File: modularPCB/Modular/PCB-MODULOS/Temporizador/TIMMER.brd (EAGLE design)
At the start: 38 x 33 mm, 8 parts

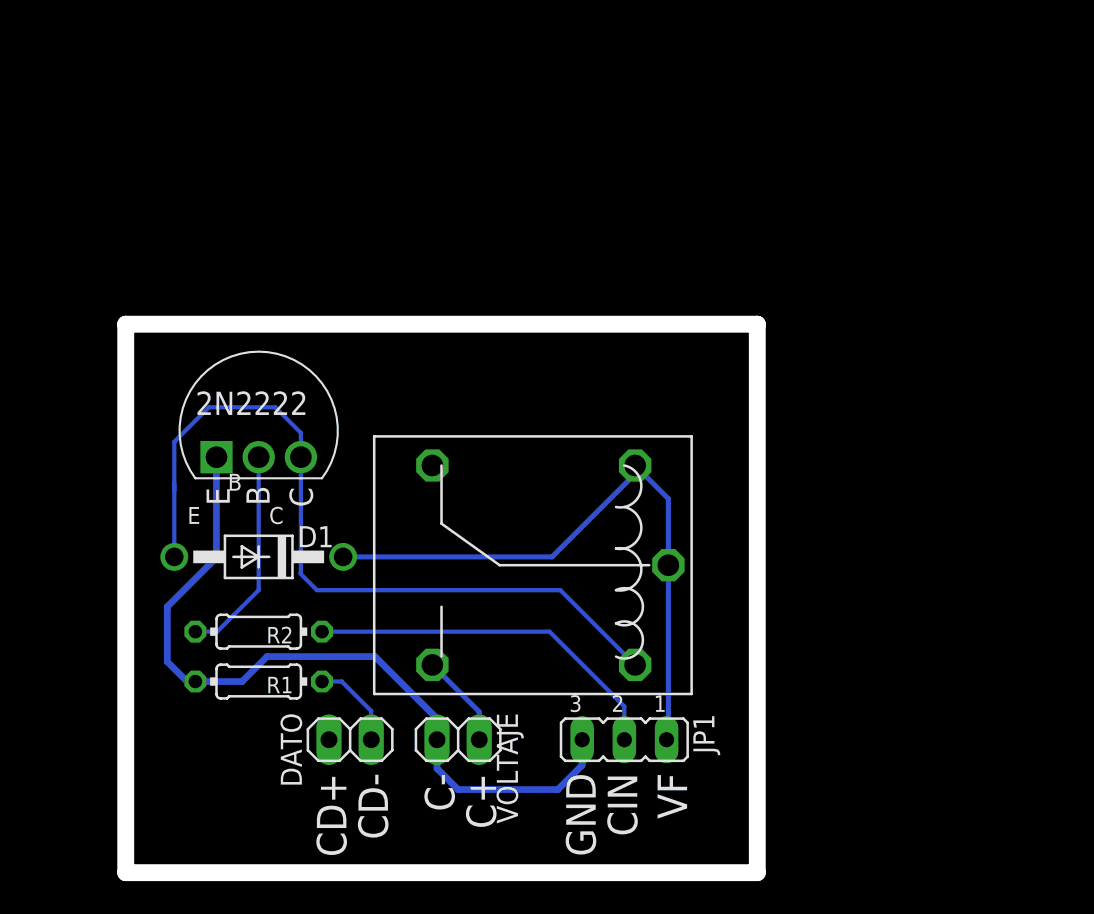
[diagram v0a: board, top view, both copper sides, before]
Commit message: Corrección de errores en pcbs
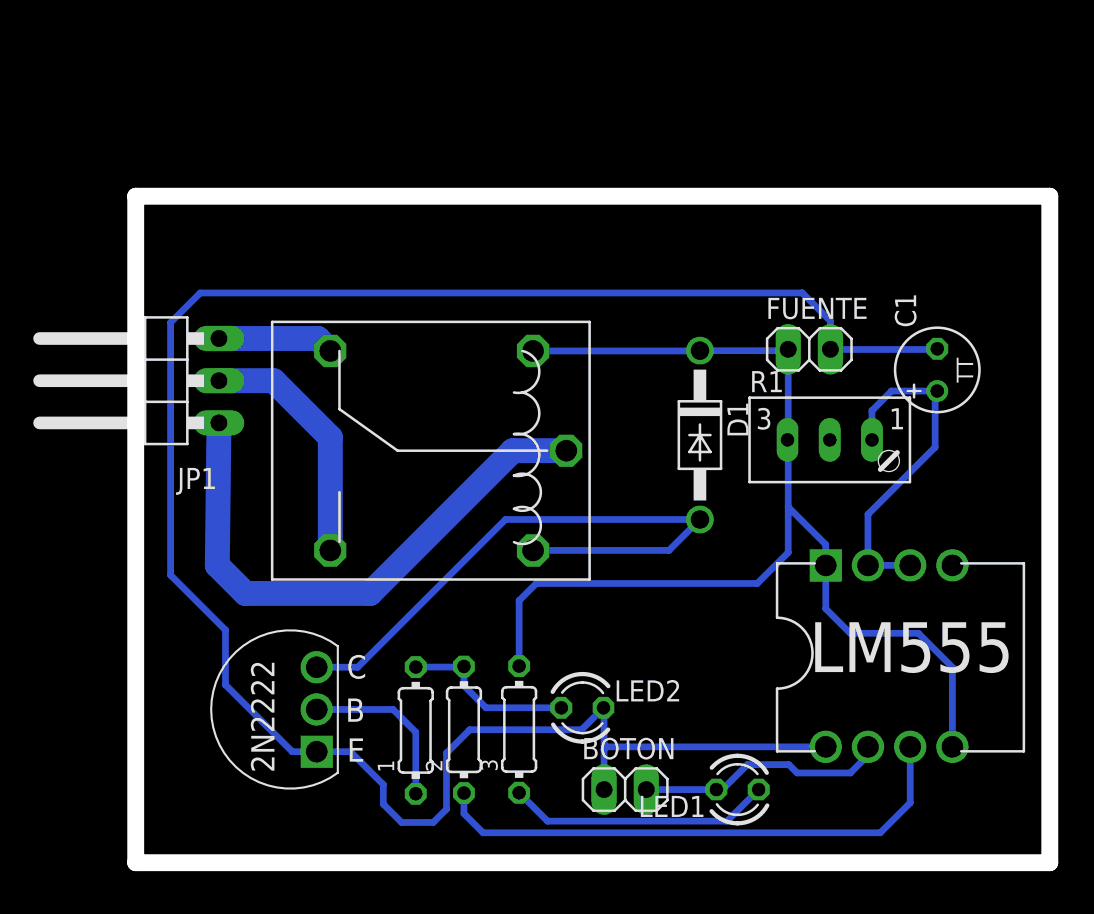
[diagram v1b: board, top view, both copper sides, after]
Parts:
- removed DATO, VOLTAJE: (no value), pinhead:1X02
- removed R2: 1k, rcl:0204/7
- added 1, 2, 3: 1k, rcl:0204/7
- added BOTON, FUENTE: (no value), pinhead:1X02
- added C1: (no value), rcl:TT2D5
- added LED1, LED2: (no value), led:LED3MM
- added U$3: RELEY, MODULAR:RELEY
- JP1: device jumper:JP2 -> pinhead:1X03/90
- R1: value 330 -> (none); device rcl:0204/7 -> pot:S64W
- U$2: value RELEY -> 555; device MODULAR:RELEY -> MODULAR:555
- moved R1 36.8 mm to (42.4, 24.8)
- moved JP1 35.5 mm to (1.80, 29.6), turned to 90 degrees
- moved D1 27.5 mm to (34.5, 26.3), turned to 270 degrees
- moved U$2 20.7 mm to (42.1, 7.57), turned to 0 degrees
- moved U$1 15.6 mm to (11.5, 9.82), turned to 90 degrees
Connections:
- removed net 3V3: DATO.2
- removed net DATO-CHAPA: DATO.1, R1.2
- removed net PULSO-CHAPA: JP1.2, R2.2
- removed net VF: D1.C, JP1.1, U$2.B2, U$2.IN
- new net N$10: C1.+, R1.A, U$2.DISCHARGE, U$2.THRESHOLD
- new net N$4: 1.1, U$1.B
- new net N$5: 1.2, 2.2, LED2.A
- new net N$6: 2.1, U$2.OUTPUT
- new net N$7: BOTON.2, LED1.K, U$2.TRIGGER
- new net N$8: 3.1, LED1.A
- new net N$9: JP1.3, U$3.NC
- new net VCC: 3.2, D1.C, FUENTE.1, R1.E, U$2.RESET, U$2.VCC, U$3.B2
- net GND: now also BOTON.1, C1.-, FUENTE.2, LED2.K, U$2.GND; no longer JP1.3, R1.1, VOLTAJE.2
- net N$1: now also D1.A, U$1.C, U$3.B1; no longer R2.1, U$1.B
- net N$2: now also JP1.1, U$3.IN; no longer D1.A, U$1.C, U$2.B1
- net N$3: now also JP1.2, U$3.NA; no longer U$2.NA, VOLTAJE.1
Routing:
- net GND: track 46.8 -> 122.5 mm
- net VCC: track 0.00 -> 70.0 mm
- net VF: track 37.5 -> 0.00 mm
- net N$6: track 0.00 -> 32.7 mm
- net N$1: track 12.8 -> 37.6 mm
- net PULSO-CHAPA: track 22.1 -> 0.00 mm
- net N$10: track 0.00 -> 20.9 mm
- net N$8: track 0.00 -> 15.9 mm
- net N$7: track 0.00 -> 15.1 mm
- net N$2: track 47.4 -> 33.8 mm
- net N$5: track 0.00 -> 10.5 mm
- net N$4: track 0.00 -> 10.2 mm
- net N$3: track 5.67 -> 14.9 mm
- net N$9: track 0.00 -> 7.15 mm
- net DATO-CHAPA: track 5.42 -> 0.00 mm
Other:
- board size 38 x 33 mm -> 55 x 40.1 mm
- board text removed: "B"
- board text removed: "C"
- board text removed: "C+"
- board text removed: "C-"
- board text removed: "CD+"
- board text removed: "CD-"
- board text removed: "CIN"
- board text removed: "E"
- board text removed: "GND"
- board text removed: "VF"

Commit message: Se agregaron brd de la ultima actualización
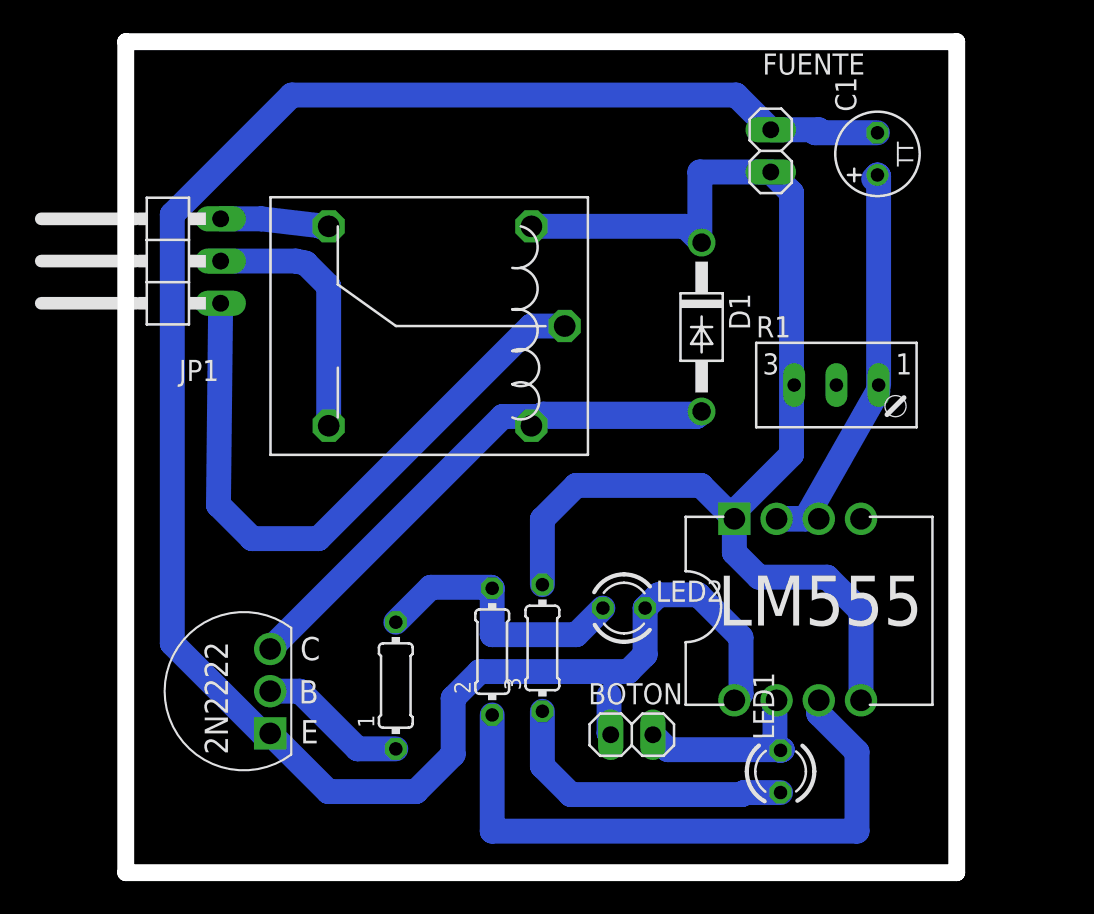
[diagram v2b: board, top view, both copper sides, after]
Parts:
- moved C1 13.5 mm to (45.2, 43.2)
- moved FUENTE 12.2 mm to (38.8, 43.4), turned to 90 degrees
- moved U$3 7.50 mm to (18.3, 32.9)
- moved JP1 7.20 mm to (1.90, 36.8)
- moved D1 6.50 mm to (34.6, 32.8)
- moved LED2 6.50 mm to (30.0, 15.9)
- moved U$2 6.17 mm to (36.6, 10.4)
- moved 3 5.10 mm to (25.1, 13.5)
- moved 2 5.00 mm to (22.1, 13.3)
- moved BOTON 3.32 mm to (30.4, 8.30)
- moved R1 3.32 mm to (42.8, 28.1)
- moved U$1 3.01 mm to (8.69, 10.9)
- moved 1 2.95 mm to (16.2, 11.3)
- moved LED1 2.81 mm to (39.4, 6.09), turned to 90 degrees
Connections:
- net VCC: no longer R1.E
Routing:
- net N$5: track 10.5 -> 16.8 mm
- net VCC: track 70.0 -> 75.4 mm
- net N$2: track 33.8 -> 39.1 mm
- net N$10: track 20.9 -> 26.1 mm
- net N$6: track 32.7 -> 37.8 mm
- net N$1: track 37.6 -> 42.5 mm
- net GND: track 122.5 -> 126.4 mm
- net N$7: track 15.1 -> 11.5 mm
- net N$8: track 15.9 -> 18.4 mm
- net N$4: track 10.2 -> 9.00 mm
- net N$3: track 14.9 -> 15.5 mm
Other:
- board size 55 x 40.1 mm -> 50 x 50 mm
